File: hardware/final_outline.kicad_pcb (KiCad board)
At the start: 2 copper layers, 99.5 x 75 mm, 36 parts, among them P1 CANCONNECTOR, P100 ISP, P101 DEBUG_LED, P2 CONN_01X14, U1 LM358N, U401 MCP2551-I/SN, U403 LPC11C14, U501 MCP1755-33, U502 MCP1755-5, U503 Zsr1000gta

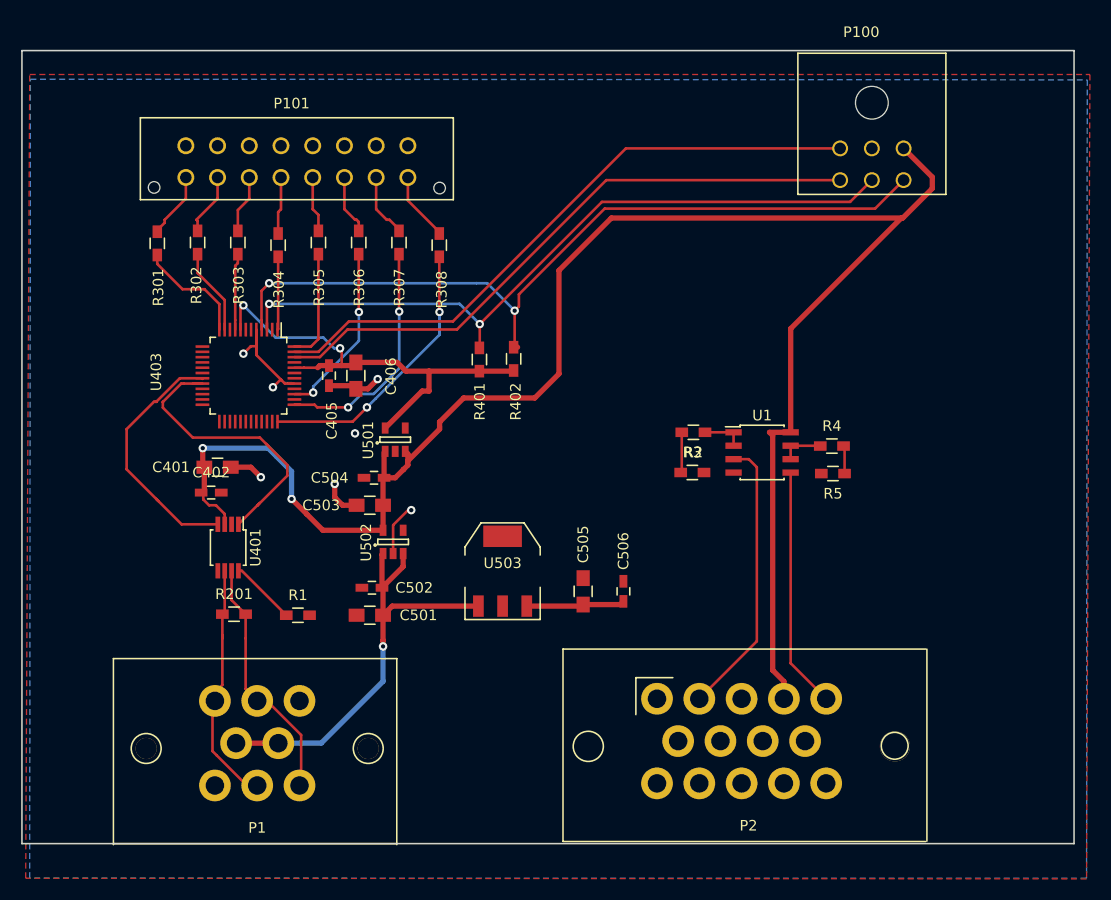
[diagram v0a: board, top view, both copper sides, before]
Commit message: still need to swap out connector
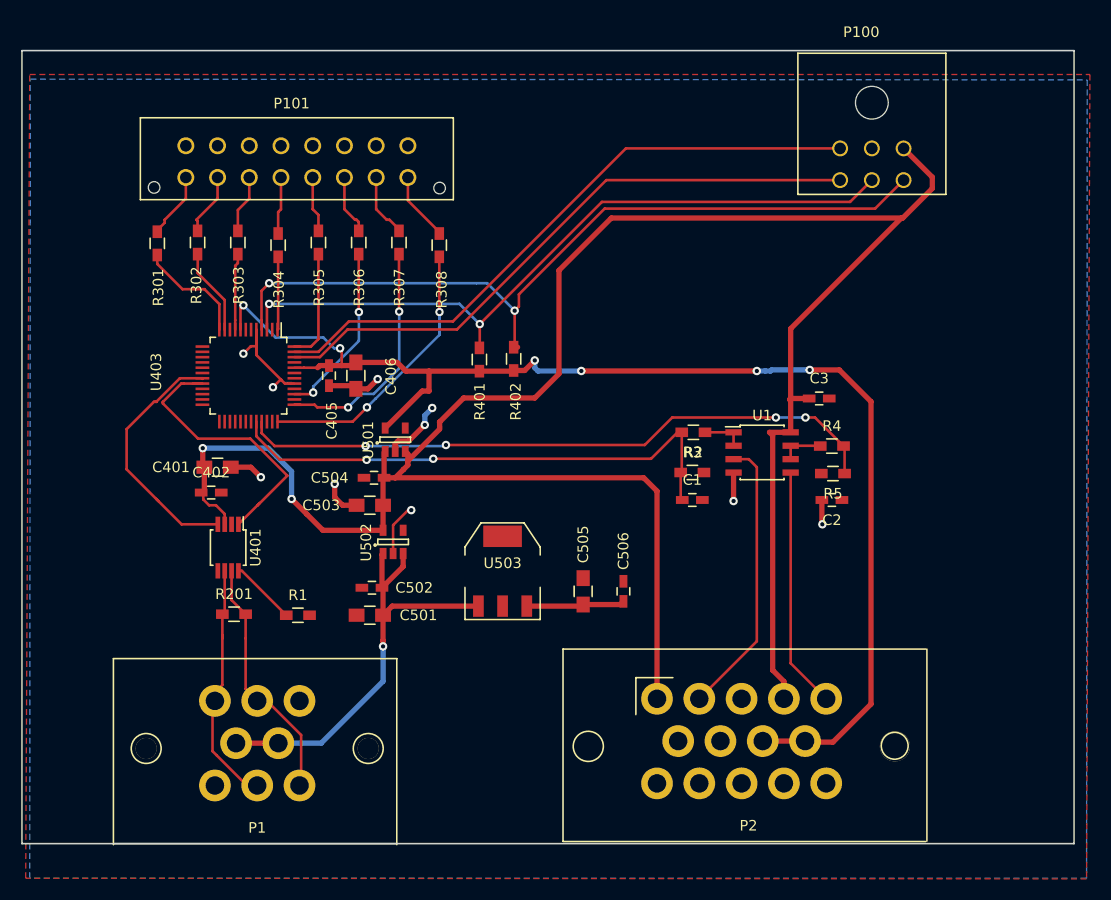
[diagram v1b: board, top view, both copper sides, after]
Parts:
- added C1: 0.1u, Capacitors_SMD:C_0603_HandSoldering, F.Cu at (165.9, 95.5)
- added C2: 0.1u, Capacitors_SMD:C_0603_HandSoldering, F.Cu at (179.1, 95.5)
- added C3: 0.1u, Capacitors_SMD:C_0603_HandSoldering, F.Cu at (177.9, 85.9)
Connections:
- P2 pad 8: Net-(P2-Pad8) -> +3V3
- P2 pad 9: Net-(P2-Pad9) -> +3V3
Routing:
- net +3V3: track 43.8 -> 120.5 mm, vias 2 -> 6
- net /Micro_Controller/TPS2_3.3V: track 2.64 -> 61.9 mm, vias 0 -> 4
- net +5V: track 165.5 -> 212.5 mm
- net /Micro_Controller/TPS1_3.3V: track 3.84 -> 50.1 mm, vias 0 -> 2
- net GND: track 29.1 -> 40.2 mm, vias 6 -> 10
- net /Micro_Controller/CAN_TXD: track 28.1 -> 27.0 mm
- net (no net): track 0.75 -> 0.63 mm, vias 1 -> 0
